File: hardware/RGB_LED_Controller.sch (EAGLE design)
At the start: 16 parts, among them IC2 MEGA8-AI, J1 POWER_JACKSLT, J2 CON_HEADER_1X04, Q1 MOSFET-NCHANNELFDD8580, Q2 MOSFET-NCHANNELFDD8580, Q4 MOSFET-NCHANNELFDD8580

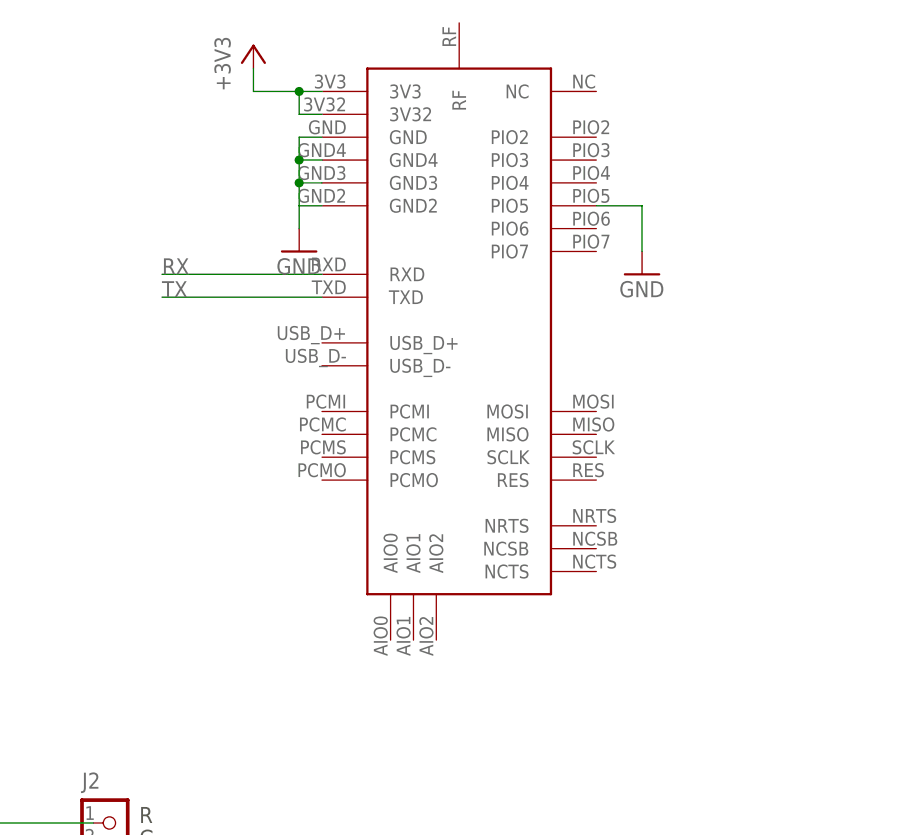
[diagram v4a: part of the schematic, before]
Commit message: Bluetooth module changed from aubtm-20 to more easily available HC-05. Footprints for through hole parts mirrored.
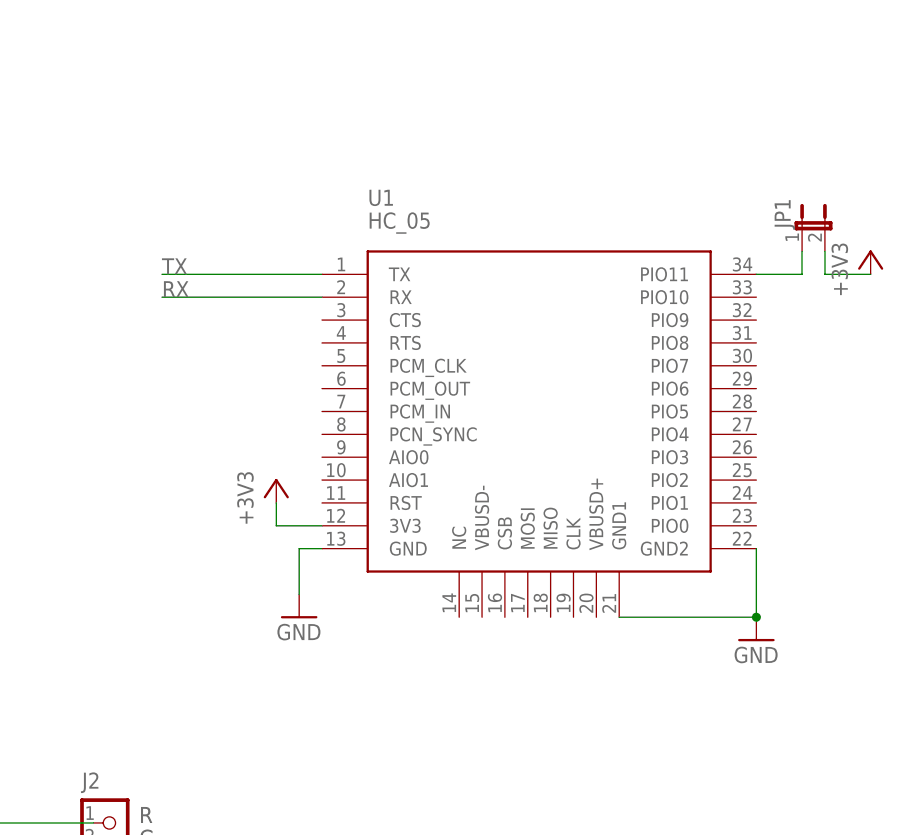
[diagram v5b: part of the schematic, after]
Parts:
- removed U$4: AUBTM-20, bluetooth:AUBTM-20
- added JP1: (no value), SparkFun:JUMPER-2-OLDSMD-NO
- added U1: HC_05, FarasbeeSerialPortBluetooth:HC_05
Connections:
- new net N$10: JP1.1, U1.PIO11
- net +3V3: now also JP1.2, U1.3V3; no longer U$4.3V3, U$4.3V32
- net GND: now also U1.GND, U1.GND1, U1.GND2; no longer U$4.GND, U$4.GND2, U$4.GND3, U$4.GND4, U$4.PIO5
- net RX: now also U1.RX; no longer U$4.RXD
- net TX: now also U1.TX; no longer U$4.TXD
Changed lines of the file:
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@@
 <part name="Q1" library="SparkFun" deviceset="MOSFET-NCHANNEL" device="FDD8580"/>
 <part name="Q2" library="SparkFun" deviceset="MOSFET-NCHANNEL" device="FDD8580"/>
-<part name="U$4" library="bluetooth" deviceset="AUBTM-20" device=""/>
 <part name="GND6" library="supply1" deviceset="GND" device=""/>
 <part name="+3V5" library="supply1" deviceset="+3V3" device=""/>
@@
 <part name="C5" library="rcl" deviceset="C-EU" device="C0603K"/>
 <part name="J2" library="dp_devices" deviceset="CON_HEADER_1X04" device=""/>
-<part name="GND7" library="supply1" deviceset="GND" device=""/>
 <part name="IC1" library="SparkFun" deviceset="V_REG_LM1117" device="SOT223"/>
 <part name="C2" library="dp_devices" deviceset="CAPACITOR_POL" device="-SMC_A" value="10uF"/>
 <part name="J1" library="SparkFun" deviceset="POWER_JACK" device="SLT"/>
 <part name="U$3" library="microbuilder" deviceset="12V" device=""/>
+<part name="U1" library="FarasbeeSerialPortBluetooth" deviceset="HC_05" device=""/>
+<part name="GND7" library="supply1" deviceset="GND" device=""/>
+<part name="JP1" library="SparkFun" deviceset="JUMPER-2-OLD" device="SMD-NO"/>
+<part name="+3V6" library="supply1" deviceset="+3V3" device=""/>
 </parts>
 <sheets>
@@
 <instance part="Q1" gate="G$1" x="58.42" y="40.64"/>
 <instance part="Q2" gate="G$1" x="58.42" y="27.94"/>
-<instance part="U$4" gate="G$1" x="127" y="121.92"/>
-<instance part="GND6" gate="1" x="109.22" y="127"/>
-<instance part="+3V5" gate="G$1" x="104.14" y="149.86"/>
+<instance part="GND6" gate="1" x="109.22" y="86.36"/>
+<instance part="+3V5" gate="G$1" x="106.68" y="101.6"/>
 <instance part="IC2" gate="G$1" x="5.08" y="55.88"/>
 <instance part="SW1" gate="G$1" x="15.24" y="88.9"/>
@@
 <instance part="C5" gate="G$1" x="-38.1" y="63.5" rot="R270"/>
 <instance part="J2" gate="J" x="86.36" y="60.96"/>
-<instance part="GND7" gate="1" x="147.32" y="124.46"/>
 <instance part="IC1" gate="G$1" x="53.34" y="111.76"/>
 <instance part="C2" gate="C" x="43.18" y="104.14"/>
 <instance part="J1" gate="G$1" x="22.86" y="104.14"/>
 <instance part="U$3" gate="G$1" x="43.18" y="124.46"/>
+<instance part="U1" gate="G$1" x="116.84" y="127"/>
+<instance part="GND7" gate="1" x="160.02" y="83.82"/>
+<instance part="JP1" gate="A" x="165.1" y="129.54"/>
+<instance part="+3V6" gate="G$1" x="172.72" y="127"/>
 </instances>
 <busses>
@@
 </segment>
 <segment>
-<pinref part="U$4" gate="G$1" pin="GND"/>
-<wire x1="111.76" y1="139.7" x2="109.22" y2="139.7" width="0.1524" layer="91"/>
-<wire x1="109.22" y1="139.7" x2="109.22" y2="137.16" width="0.1524" layer="91"/>
-<pinref part="U$4" gate="G$1" pin="GND4"/>
-<wire x1="109.22" y1="137.16" x2="111.76" y2="137.16" width="0.1524" layer="91"/>
-<pinref part="U$4" gate="G$1" pin="GND3"/>
-<wire x1="111.76" y1="134.62" x2="109.22" y2="134.62" width="0.1524" layer="91"/>
-<wire x1="109.22" y1="134.62" x2="109.22" y2="137.16" width="0.1524" layer="91"/>
-<pinref part="U$4" gate="G$1" pin="GND2"/>
-<wire x1="111.76" y1="132.08" x2="109.22" y2="132.08" width="0.1524" layer="91"/>
-<wire x1="109.22" y1="132.08" x2="109.22" y2="134.62" width="0.1524" layer="91"/>
-<junction x="109.22" y="137.16"/>
-<junction x="109.22" y="134.62"/>
-<wire x1="109.22" y1="132.08" x2="109.22" y2="129.54" width="0.1524" layer="91"/>
-<pinref part="GND6" gate="1" pin="GND"/>
-</segment>
-<segment>
-<pinref part="U$4" gate="G$1" pin="PIO5"/>
-<pinref part="GND7" gate="1" pin="GND"/>
-<wire x1="142.24" y1="132.08" x2="147.32" y2="132.08" width="0.1524" layer="91"/>
-<wire x1="147.32" y1="132.08" x2="147.32" y2="127" width="0.1524" layer="91"/>
-</segment>
-<segment>
 <pinref part="J1" gate="G$1" pin="GNDBREAK"/>
 <pinref part="J1" gate="G$1" pin="GND"/>
@@
 <wire x1="25.4" y1="106.68" x2="30.48" y2="106.68" width="0.1524" layer="91"/>
 <wire x1="30.48" y1="106.68" x2="30.48" y2="104.14" width="0.1524" layer="91"/>
+</segment>
+<segment>
+<pinref part="GND6" gate="1" pin="GND"/>
+<wire x1="109.22" y1="88.9" x2="109.22" y2="93.98" width="0.1524" layer="91"/>
+<pinref part="U1" gate="G$1" pin="GND"/>
+<wire x1="109.22" y1="93.98" x2="111.76" y2="93.98" width="0.1524" layer="91"/>
+</segment>
+<segment>
+<pinref part="U1" gate="G$1" pin="GND1"/>
+<pinref part="U1" gate="G$1" pin="GND2"/>
+<wire x1="144.78" y1="86.36" x2="160.02" y2="86.36" width="0.1524" layer="91"/>
+<wire x1="160.02" y1="86.36" x2="160.02" y2="93.98" width="0.1524" layer="91"/>
+<pinref part="GND7" gate="1" pin="GND"/>
+<junction x="160.02" y="86.36"/>
 </segment>
 </net>
@@
 </segment>
 <segment>
-<pinref part="U$4" gate="G$1" pin="3V32"/>
-<wire x1="111.76" y1="142.24" x2="109.22" y2="142.24" width="0.1524" layer="91"/>
-<wire x1="109.22" y1="142.24" x2="109.22" y2="144.78" width="0.1524" layer="91"/>
-<pinref part="U$4" gate="G$1" pin="3V3"/>
-<wire x1="109.22" y1="144.78" x2="111.76" y2="144.78" width="0.1524" layer="91"/>
-<wire x1="109.22" y1="144.78" x2="104.14" y2="144.78" width="0.1524" layer="91"/>
 <pinref part="+3V5" gate="G$1" pin="+3V3"/>
-<wire x1="104.14" y1="147.32" x2="104.14" y2="144.78" width="0.1524" layer="91"/>
-<junction x="109.22" y="144.78"/>
+<wire x1="106.68" y1="99.06" x2="106.68" y2="96.52" width="0.1524" layer="91"/>
+<pinref part="U1" gate="G$1" pin="3V3"/>
+<wire x1="106.68" y1="96.52" x2="111.76" y2="96.52" width="0.1524" layer="91"/>
+</segment>
+<segment>
+<pinref part="JP1" gate="A" pin="2"/>
+<wire x1="167.64" y1="127" x2="167.64" y2="124.46" width="0.1524" layer="91"/>
+<wire x1="167.64" y1="124.46" x2="172.72" y2="124.46" width="0.1524" layer="91"/>
+<pinref part="+3V6" gate="G$1" pin="+3V3"/>
 </segment>
 </net>
@@
 </segment>
 <segment>
-<pinref part="U$4" gate="G$1" pin="TXD"/>
-<wire x1="111.76" y1="121.92" x2="93.98" y2="121.92" width="0.1524" layer="91"/>
-<label x="93.98" y="121.92" size="1.778" layer="95"/>
+<wire x1="111.76" y1="124.46" x2="93.98" y2="124.46" width="0.1524" layer="91"/>
+<label x="93.98" y="124.46" size="1.778" layer="95"/>
+<pinref part="U1" gate="G$1" pin="TX"/>
 </segment>
 </net>
@@
 </segment>
 <segment>
-<pinref part="U$4" gate="G$1" pin="RXD"/>
-<wire x1="111.76" y1="124.46" x2="93.98" y2="124.46" width="0.1524" layer="91"/>
-<label x="93.98" y="124.46" size="1.778" layer="95"/>
+<wire x1="111.76" y1="121.92" x2="93.98" y2="121.92" width="0.1524" layer="91"/>
+<label x="93.98" y="121.92" size="1.778" layer="95"/>
+<pinref part="U1" gate="G$1" pin="RX"/>
 </segment>
 </net>
@@
 </segment>
 </net>
+<net name="N$10" class="0">
+<segment>
+<pinref part="U1" gate="G$1" pin="PIO11"/>
+<pinref part="JP1" gate="A" pin="1"/>
+<wire x1="160.02" y1="124.46" x2="165.1" y2="124.46" width="0.1524" layer="91"/>
+<wire x1="165.1" y1="124.46" x2="165.1" y2="127" width="0.1524" layer="91"/>
+</segment>
+</net>

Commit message: rev 3 PCB. Printout taken
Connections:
- new net N$11: J2.4
- net 12V: no longer J2.4
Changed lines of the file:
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@@
 <part name="GND2" library="supply1" deviceset="GND" device=""/>
 <part name="GND3" library="supply1" deviceset="GND" device=""/>
-<part name="U$2" library="microbuilder" deviceset="12V" device=""/>
 <part name="+3V2" library="supply1" deviceset="+3V3" device=""/>
 <part name="GND4" library="supply1" deviceset="GND" device=""/>
@@
 <instance part="GND2" gate="1" x="30.48" y="101.6"/>
 <instance part="GND3" gate="1" x="66.04" y="17.78"/>
-<instance part="U$2" gate="G$1" x="91.44" y="45.72"/>
 <instance part="+3V2" gate="G$1" x="-20.32" y="25.4" rot="R180"/>
 <instance part="GND4" gate="1" x="-30.48" y="25.4"/>
@@
 <net name="12V" class="0">
 <segment>
-<wire x1="86.36" y1="55.88" x2="81.28" y2="55.88" width="0.1524" layer="91"/>
-<wire x1="81.28" y1="55.88" x2="81.28" y2="45.72" width="0.1524" layer="91"/>
-<wire x1="81.28" y1="45.72" x2="91.44" y2="45.72" width="0.1524" layer="91"/>
-<pinref part="U$2" gate="G$1" pin="12V"/>
-<pinref part="J2" gate="J" pin="4"/>
-</segment>
-<segment>
 <wire x1="43.18" y1="111.76" x2="45.72" y2="111.76" width="0.1524" layer="91"/>
 <wire x1="43.18" y1="111.76" x2="43.18" y2="124.46" width="0.1524" layer="91"/>
@@
 </segment>
 </net>
+<net name="N$11" class="0">
+<segment>
+<wire x1="86.36" y1="55.88" x2="81.28" y2="55.88" width="0.1524" layer="91"/>
+<wire x1="81.28" y1="55.88" x2="81.28" y2="45.72" width="0.1524" layer="91"/>
+<wire x1="81.28" y1="45.72" x2="91.44" y2="45.72" width="0.1524" layer="91"/>
+<pinref part="J2" gate="J" pin="4"/>
+</segment>
+</net>
